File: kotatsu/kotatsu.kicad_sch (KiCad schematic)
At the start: 81 parts, among them SW1 SW_Push, SW10 SW_Push, SW11 SW_Push, SW12 SW_Push, SW13 SW_Push, SW14 SW_Push, SW15 SW_Push, SW16 SW_Push, SW17 SW_Push, SW18 SW_Push, SW19 SW_Push, SW2 SW_Push, SW20 SW_Push, SW21 SW_Push, SW22 SW_Push, SW23 SW_Push, SW24 SW_Push, SW25 SW_Push, SW26 SW_Push, SW27 SW_Push, SW28 SW_Push, SW29 SW_Push, SW3 SW_Push, SW30 SW_Push, SW31 SW_Push, SW32 SW_Push, SW33 SW_Push, SW34 SW_Push, SW35 SW_Push, SW36 SW_Push, SW37 SW_Push, SW38 SW_Push, SW39 SW_Push, SW4 SW_Push, SW40 SW_Push, SW5 SW_Push, SW6 SW_Push, SW7 SW_Push, SW8 SW_Push, SW9 SW_Push, U1 Pico

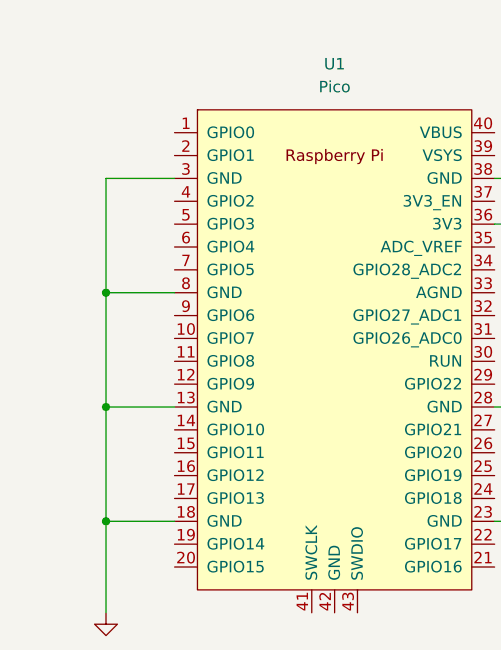
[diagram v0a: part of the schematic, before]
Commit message: add labels to pico
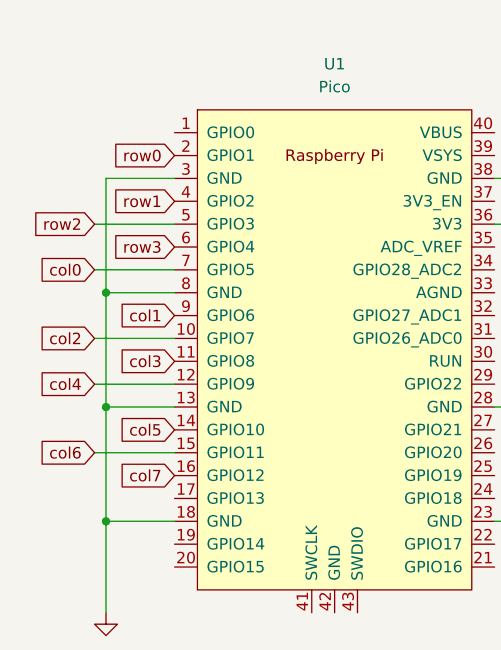
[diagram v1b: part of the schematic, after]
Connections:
- net col0: now also U1.7 (GPIO5)
- net col1: now also U1.9 (GPIO6)
- net col2: now also U1.10 (GPIO7)
- net col3: now also U1.11 (GPIO8)
- net col4: now also U1.12 (GPIO9)
- net col5: now also U1.14 (GPIO10)
- net col6: now also U1.15 (GPIO11)
- net col7: now also U1.16 (GPIO12)
- net row0: now also U1.2 (GPIO1)
- net row1: now also U1.4 (GPIO2)
- net row2: now also U1.5 (GPIO3)
- net row3: now also U1.6 (GPIO4)

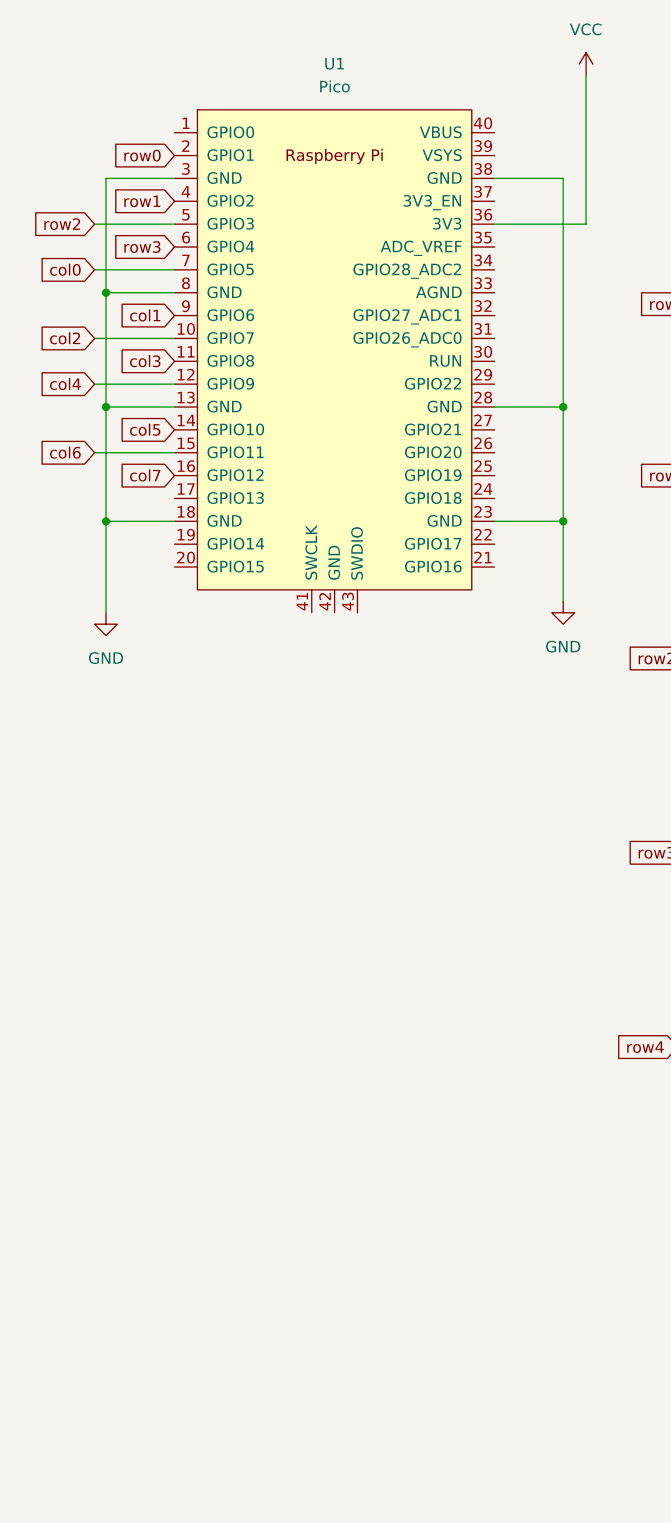
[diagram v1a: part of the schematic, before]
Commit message: 回路図エディタ側の作業を完了した
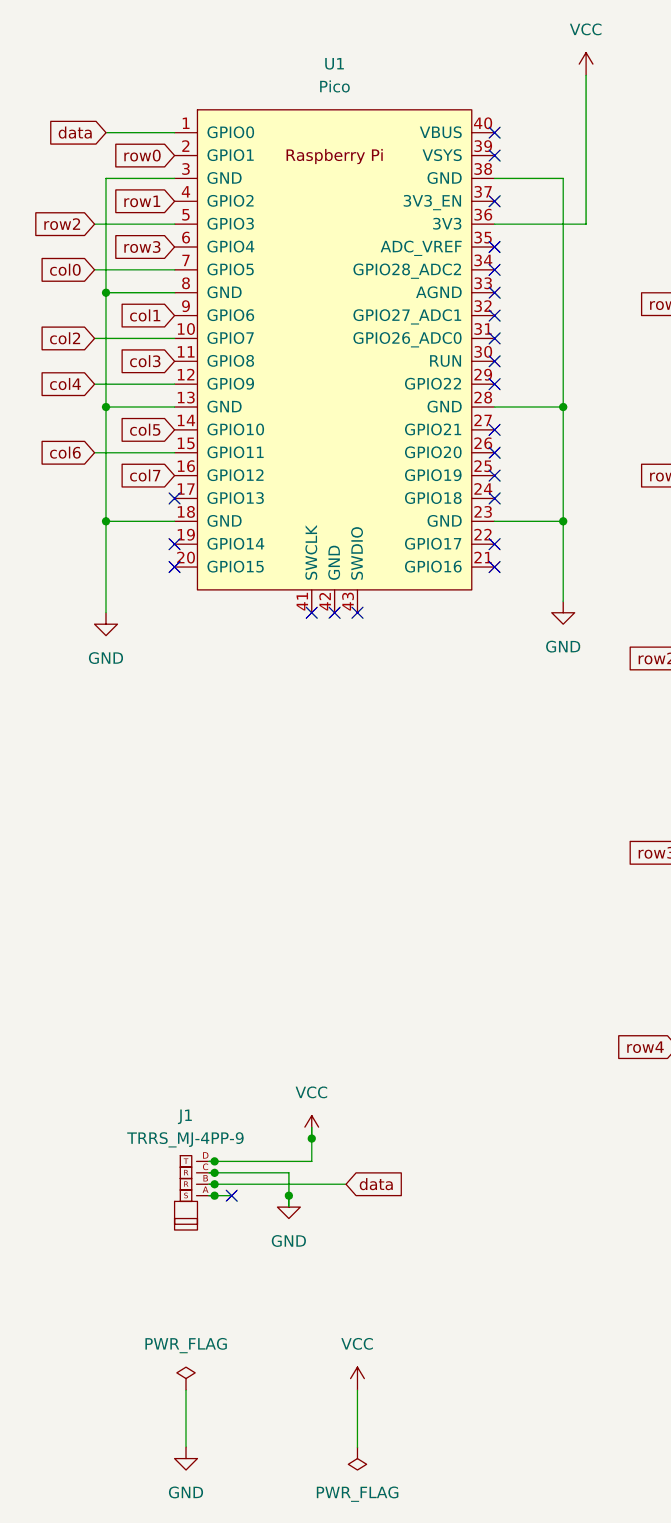
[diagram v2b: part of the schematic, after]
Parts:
- added J1: TRRS_MJ-4PP-9, symbol Salicylic_kbd:TRRS_MJ-4PP-9
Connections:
- net GND: now also J1.C
- net VCC: now also J1.D
- net data: now reaches U1.1 (GPIO0)
- net data: now also J1.B
- no-connect marks 0 -> 23

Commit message: Circuit editing completed
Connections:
- net data: now also U1.17 (GPIO13)
- no-connect marks 23 -> 22
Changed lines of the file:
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@@
-	)
-	(no_connect
-		(at 31.75 67.31)
 	)
 	(no_connect
@@
 	(wire
 		(pts
+			(xy 22.86 67.31) (xy 31.75 67.31)
+		)
+		(stroke
+			(width 0)
+			(type default)
+		)
+	)
+	(wire
+		(pts
 			(xy 67.31 69.85) (xy 74.93 69.85)
 		)
@@
 			(effects
 				(font
+					(size 1.27 1.27)
+				)
+				(justify right)
+				(hide yes)
+			)
+		)
+	)
+	(global_label "data"
+		(shape input)
+		(at 22.86 67.31 180)
+		(fields_autoplaced yes)
+		(effects
+			(font
+				(size 1.27 1.27)
+			)
+			(justify right)
+		)
+		(property "Intersheetrefs" "${INTERSHEET_REFS}"
+			(at 15.7021 67.31 0)
+			(effects
+				(font

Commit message: RXTXマスター
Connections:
- net col0: now also U1.9 (GPIO6); no longer U1.7 (GPIO5)
- net col1: now also U1.10 (GPIO7); no longer U1.9 (GPIO6)
- net col2: now also U1.11 (GPIO8); no longer U1.10 (GPIO7)
- net col3: now also U1.12 (GPIO9); no longer U1.11 (GPIO8)
- net col4: now also U1.14 (GPIO10); no longer U1.12 (GPIO9)
- net col5: now also U1.15 (GPIO11); no longer U1.14 (GPIO10)
- net col6: now also U1.16 (GPIO12); no longer U1.15 (GPIO11)
- net col7: now also U1.17 (GPIO13); no longer U1.16 (GPIO12)
- net row0: now also U1.4 (GPIO2); no longer U1.2 (GPIO1)
- net row1: now also U1.5 (GPIO3); no longer U1.4 (GPIO2)
- net row2: now also U1.6 (GPIO4); no longer U1.5 (GPIO3)
- net row3: now also U1.7 (GPIO5); no longer U1.6 (GPIO4)
- net RX: now reaches J1.A
- net RX: now also U1.2 (GPIO1)
- net data renamed TX
- net TX: no longer U1.17 (GPIO13)
- no-connect marks 22 -> 21

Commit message: add kotatsu_right
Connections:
- net RX: now also U1.1 (GPIO0); no longer U1.2 (GPIO1)
- net TX: now also U1.2 (GPIO1); no longer U1.1 (GPIO0)
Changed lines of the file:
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@@
-	(wire
-		(pts
-			(xy 20.32 29.21) (xy 31.75 29.21)
-		)
-		(stroke
-			(width 0)
-			(type default)
-		)
-	)
 	(wire
 		(pts
@@
 	(wire
 		(pts
+			(xy 26.67 26.67) (xy 31.75 26.67)
+		)
+		(stroke
+			(width 0)
+			(type default)
+		)
+	)
+	(wire
+		(pts
 			(xy 46.99 138.43) (xy 46.99 140.97)
 		)
@@
 	(global_label "RX"
 		(shape input)
-		(at 20.32 29.21 180)
-		(fields_autoplaced yes)
-		(effects
-			(font
-				(size 1.27 1.27)
-			)
-			(justify right)
-		)
-		(property "Intersheetrefs" "${INTERSHEET_REFS}"
-			(at 14.8553 29.21 0)
+		(at 26.67 26.67 180)
+		(fields_autoplaced yes)
+		(effects
+			(font
+				(size 1.27 1.27)
+			)
+			(justify right)
+		)
+		(property "Intersheetrefs" "${INTERSHEET_REFS}"
+			(at 21.2053 26.67 0)
 			(effects
 				(font
@@
 	(global_label "TX"
 		(shape input)
-		(at 31.75 26.67 180)
-		(fields_autoplaced yes)
-		(effects
-			(font
-				(size 1.27 1.27)
-			)
-			(justify right)
-		)
-		(property "Intersheetrefs" "${INTERSHEET_REFS}"
-			(at 26.5877 26.67 0)
-			(effects
-				(font
+		(at 31.75 29.21 180)
+		(fields_autoplaced yes)
+		(effects
+			(font
+				(size 1.27 1.27)
+			)
+			(justify right)
+		)
+		(property "Intersheetrefs" "${INTERSHEET_REFS}"
+			(at 26.5877 29.21 0)
+			(effects
+				(font

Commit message: wiring ongoing
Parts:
- D1, D10, D11, D12, D13, D14, D15, D16, D17, D18, D19, D2, D20, D21, D22, D23, D24, D25, D26, D27, D28, D29, D3, D30, D31, D32, D33, D34, D35, D36, D37, D38, D39, D4, D40, D5, D6, D7, D8, D9: footprint (none) -> Diode_SMD:D_MELF-RM10_Universal_Handsoldering
- J1: footprint (none) -> kbd_Parts:TRRS_MJ-4PP-9
- SW1, SW17, SW25, SW9: footprint (none) -> Button_Switch_Keyboard:SW_Cherry_MX_1.75u_PCB
- SW10, SW11, SW12, SW13, SW14, SW15, SW16, SW18, SW19, SW2, SW20, SW21, SW22, SW23, SW24, SW26, SW27, SW28, SW29, SW3, SW30, SW31, SW33, SW34, SW35, SW37, SW38, SW39, SW4, SW40, SW5, SW6, SW7, SW8: footprint (none) -> Button_Switch_Keyboard:SW_Cherry_MX_1.00u_PCB
- SW32: footprint (none) -> Button_Switch_Keyboard:SW_Cherry_MX_2.00u_Vertical_PCB
- SW36: footprint (none) -> Button_Switch_Keyboard:SW_Cherry_MX_2.00u_PCB
- U1: footprint RPi_Pico:RPi_Pico_SMD_TH -> Module:RaspberryPi_Pico_SMD

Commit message: bangyo
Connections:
- net RX: now also U1.2 (GPIO1); no longer U1.1 (GPIO0)
- net TX: now also U1.1 (GPIO0); no longer U1.2 (GPIO1)
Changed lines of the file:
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@@
+	(wire
+		(pts
+			(xy 29.21 29.21) (xy 31.75 29.21)
+		)
+		(stroke
+			(width 0)
+			(type default)
+		)
+	)
 	(wire
 		(pts
@@
 	(wire
 		(pts
+			(xy 24.13 26.67) (xy 31.75 26.67)
+		)
+		(stroke
+			(width 0)
+			(type default)
+		)
+	)
+	(wire
+		(pts
 			(xy 242.57 77.47) (xy 242.57 99.06)
 		)
@@
 	(wire
 		(pts
-			(xy 26.67 26.67) (xy 31.75 26.67)
-		)
-		(stroke
-			(width 0)
-			(type default)
-		)
-	)
-	(wire
-		(pts
 			(xy 46.99 138.43) (xy 46.99 140.97)
 		)
@@
 	(global_label "RX"
 		(shape input)
-		(at 26.67 26.67 180)
-		(fields_autoplaced yes)
-		(effects
-			(font
-				(size 1.27 1.27)
-			)
-			(justify right)
-		)
-		(property "Intersheetrefs" "${INTERSHEET_REFS}"
-			(at 21.2053 26.67 0)
+		(at 29.21 29.21 180)
+		(fields_autoplaced yes)
+		(effects
+			(font
+				(size 1.27 1.27)
+			)
+			(justify right)
+		)
+		(property "Intersheetrefs" "${INTERSHEET_REFS}"
+			(at 23.7453 29.21 0)
 			(effects
 				(font
@@
 	(global_label "TX"
 		(shape input)
-		(at 31.75 29.21 180)
-		(fields_autoplaced yes)
-		(effects
-			(font
-				(size 1.27 1.27)
-			)
-			(justify right)
-		)
-		(property "Intersheetrefs" "${INTERSHEET_REFS}"
-			(at 26.5877 29.21 0)
-			(effects
-				(font
+		(at 24.13 26.67 180)
+		(fields_autoplaced yes)
+		(effects
+			(font
+				(size 1.27 1.27)
+			)
+			(justify right)
+		)
+		(property "Intersheetrefs" "${INTERSHEET_REFS}"
+			(at 18.9677 26.67 0)
+			(effects
+				(font
